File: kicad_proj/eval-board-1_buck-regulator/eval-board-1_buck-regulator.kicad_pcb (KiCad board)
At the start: 4 copper layers, 57.2 x 37 mm, 50 parts, among them J1 Conn_01x02, J2 Conn_01x06, J3 Conn_01x02, U1 SIC453ED-T1-GE3

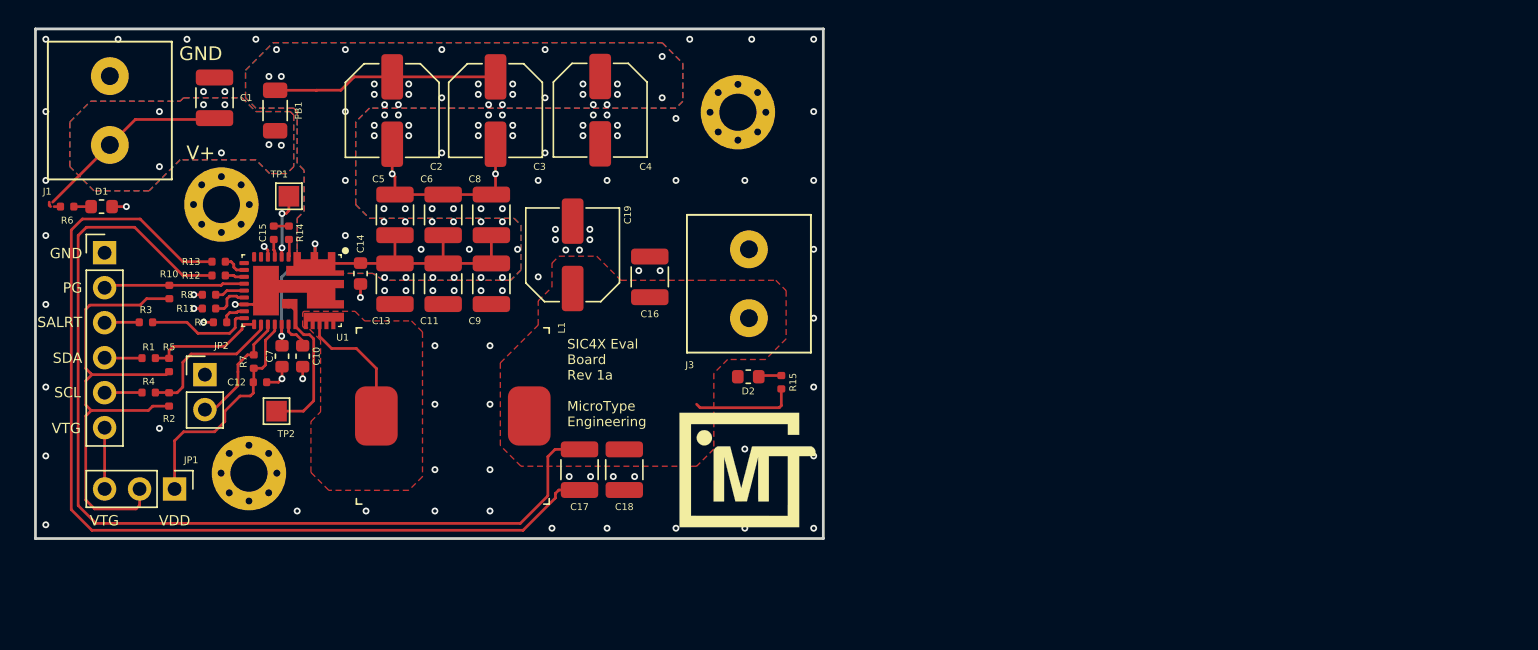
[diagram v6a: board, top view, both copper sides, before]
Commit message: Minor adjust to refdes for clarity, add labels to leds
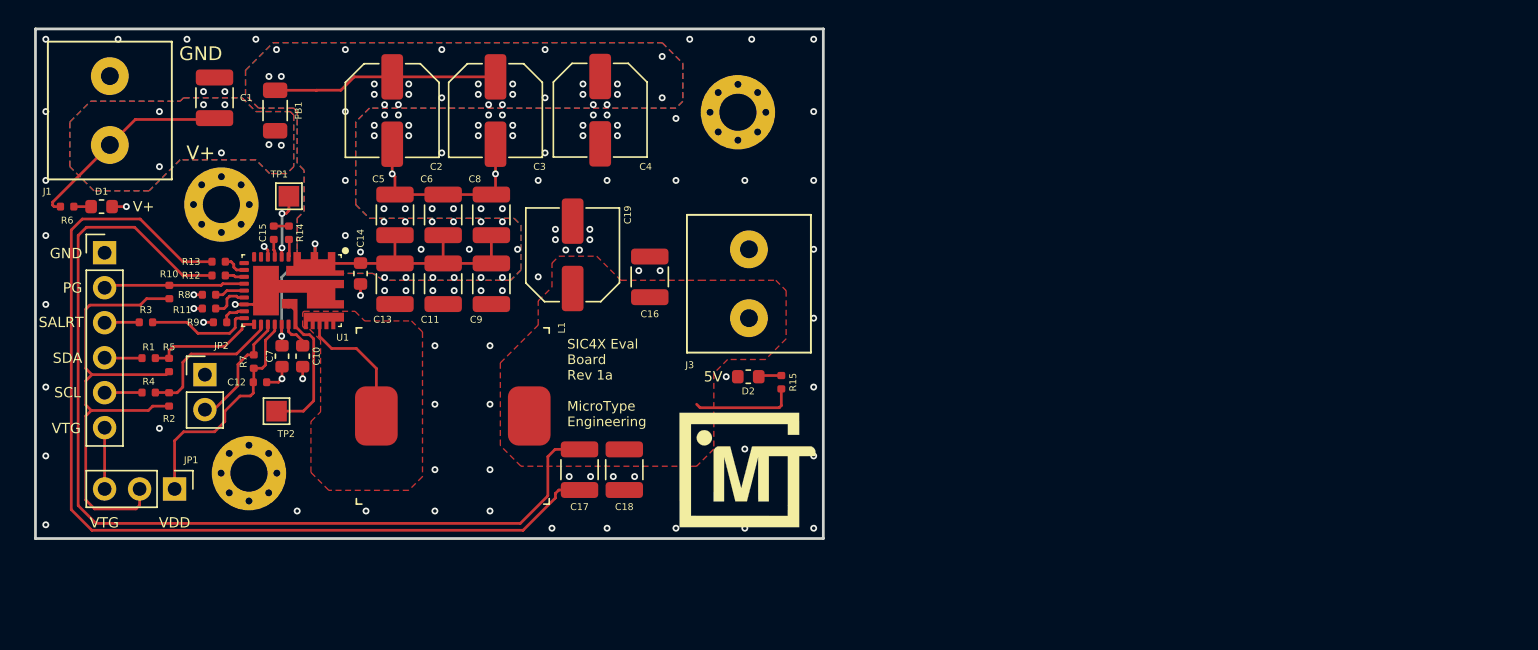
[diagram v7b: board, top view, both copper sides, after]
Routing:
- net GND: track 99.9 -> 99.5 mm, vias 100 -> 101
- net Net-(C11-Pad1): track 47.5 -> 47.4 mm, vias 48 -> 49
- added copper zone on B.Cu, net GND
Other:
- board text added: "5V"
